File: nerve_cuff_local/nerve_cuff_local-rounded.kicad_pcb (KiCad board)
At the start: 2 copper layers, 4 x 5.3 mm, 2 parts

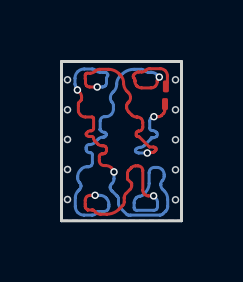
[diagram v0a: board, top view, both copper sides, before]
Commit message: cleaning up XY gradient board, updating pads
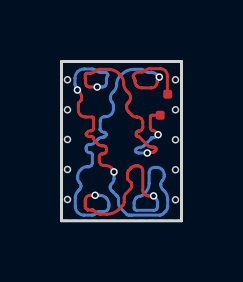
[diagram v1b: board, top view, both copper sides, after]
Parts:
- removed the REF** at (131.1, 65.3)
- removed the REF** at (131.1, 65.9)
- added REF**: small_pad_nerve_cuff, nerve_cuff_pads:small_pad_nerve_cuff, F.Cu at (130.5, 66.2)
- added REF**: small_pad_nerve_cuff, nerve_cuff_pads:small_pad_nerve_cuff, F.Cu at (130.7, 65.5)
